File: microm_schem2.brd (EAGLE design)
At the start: 101.6 x 81.3 mm, 77 parts, among them Q1 16 MHz

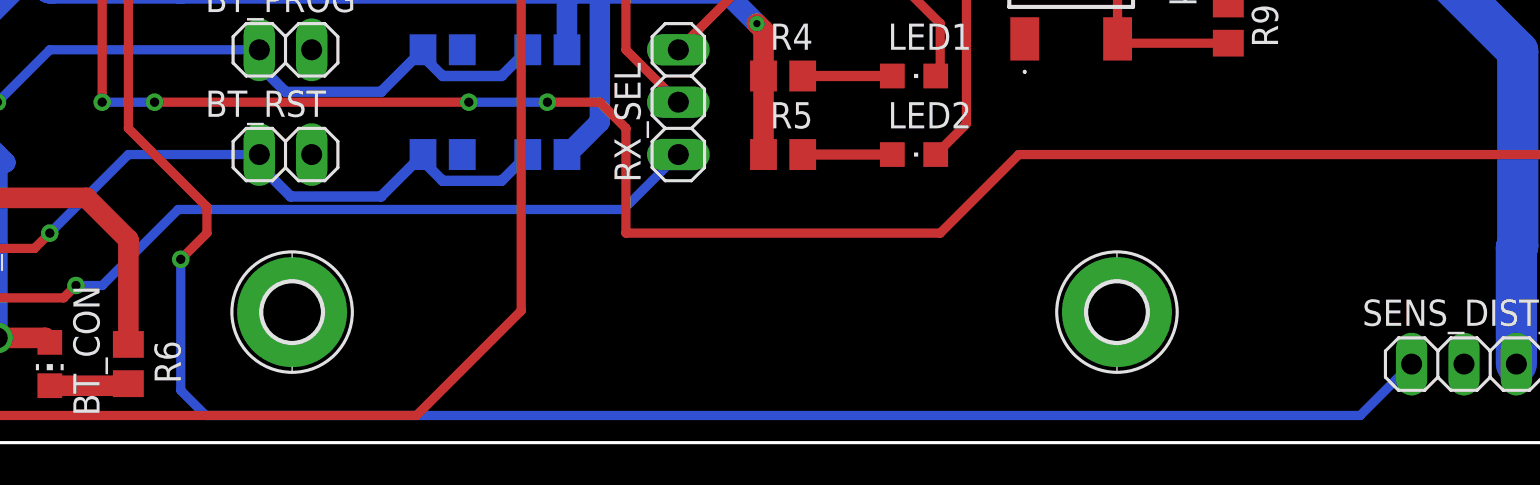
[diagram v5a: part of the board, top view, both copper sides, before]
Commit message: Fix overlapping uart and sensor routes
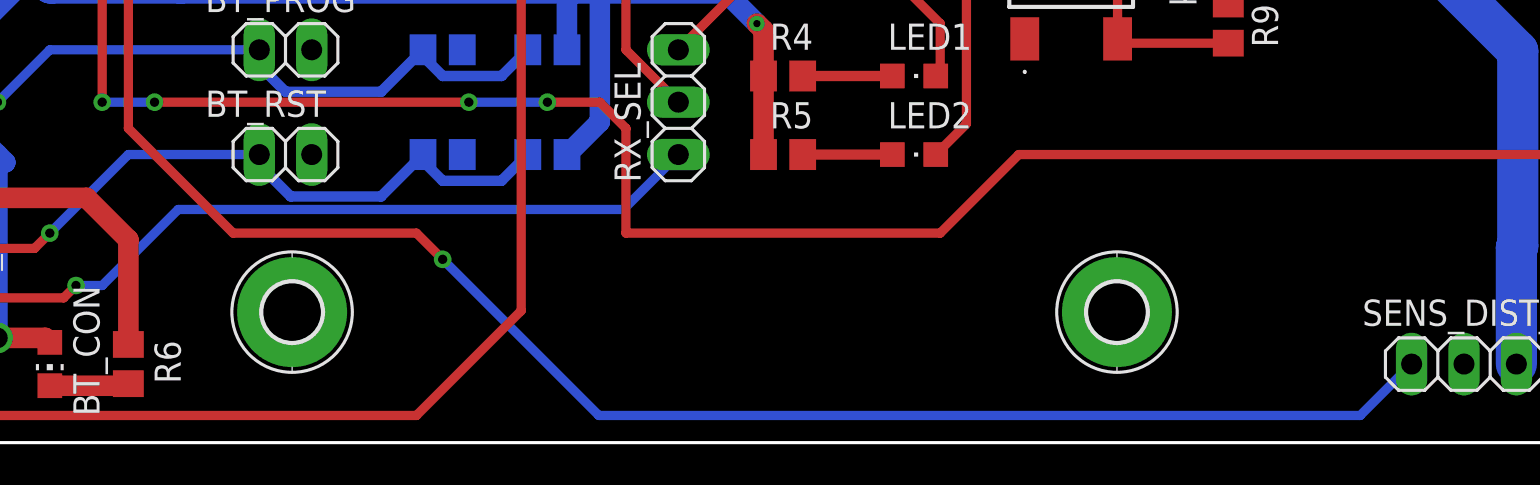
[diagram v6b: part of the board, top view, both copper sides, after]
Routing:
- net SENS_DIST_3: track 98.5 -> 91.5 mm
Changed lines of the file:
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@@
 <wire x1="29.68" y1="32.22" x2="22.86" y2="25.4" width="0.45" layer="1"/>
 <wire x1="22.86" y1="25.4" x2="22.86" y2="15.24" width="0.45" layer="1"/>
-<wire x1="22.86" y1="15.24" x2="26.67" y2="11.43" width="0.45" layer="1"/>
-<wire x1="26.67" y1="11.43" x2="26.67" y2="10.16" width="0.45" layer="1"/>
-<wire x1="26.67" y1="10.16" x2="25.4" y2="8.89" width="0.45" layer="1"/>
-<via x="25.4" y="8.89" extent="1-16" drill="0.45"/>
-<wire x1="25.4" y1="8.89" x2="25.4" y2="2.54" width="0.45" layer="16"/>
-<wire x1="25.4" y1="2.54" x2="26.6228" y2="1.3172" width="0.45" layer="16"/>
-<wire x1="82.5972" y1="1.3172" x2="85.09" y2="3.81" width="0.45" layer="16"/>
-<wire x1="26.6228" y1="1.3172" x2="82.5972" y2="1.3172" width="0.45" layer="16"/>
+<wire x1="22.86" y1="15.24" x2="27.94" y2="10.16" width="0.45" layer="1"/>
+<wire x1="85.09" y1="3.81" x2="82.5972" y2="1.3172" width="0.45" layer="16"/>
+<wire x1="82.5972" y1="1.3172" x2="45.6728" y2="1.3172" width="0.45" layer="16"/>
+<wire x1="45.6728" y1="1.3172" x2="38.1" y2="8.89" width="0.45" layer="16"/>
+<via x="38.1" y="8.89" extent="1-16" drill="0.45"/>
+<wire x1="38.1" y1="8.89" x2="36.83" y2="10.16" width="0.45" layer="1"/>
+<wire x1="36.83" y1="10.16" x2="27.94" y2="10.16" width="0.45" layer="1"/>
 </signal>
 <signal name="SENS_DIST_2">
